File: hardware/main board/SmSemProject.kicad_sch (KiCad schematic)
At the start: 11 parts, among them J1 Conn_01x06, J2 Conn_01x06, J3 Conn_01x02

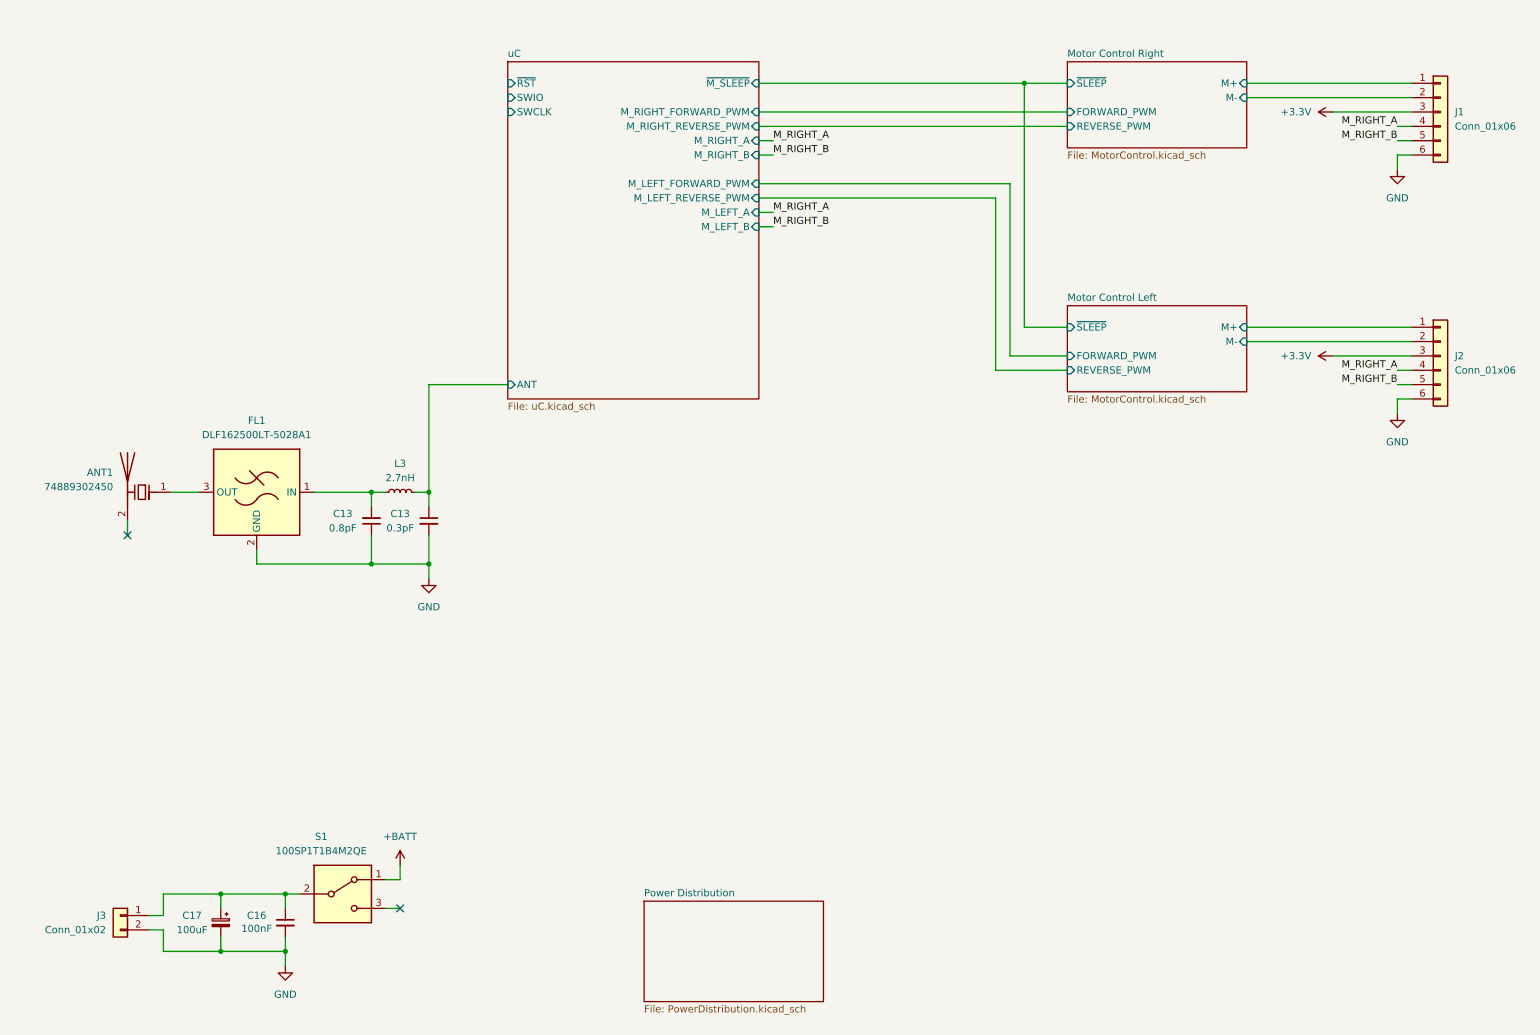
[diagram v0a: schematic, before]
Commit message: main board done, added front board projec
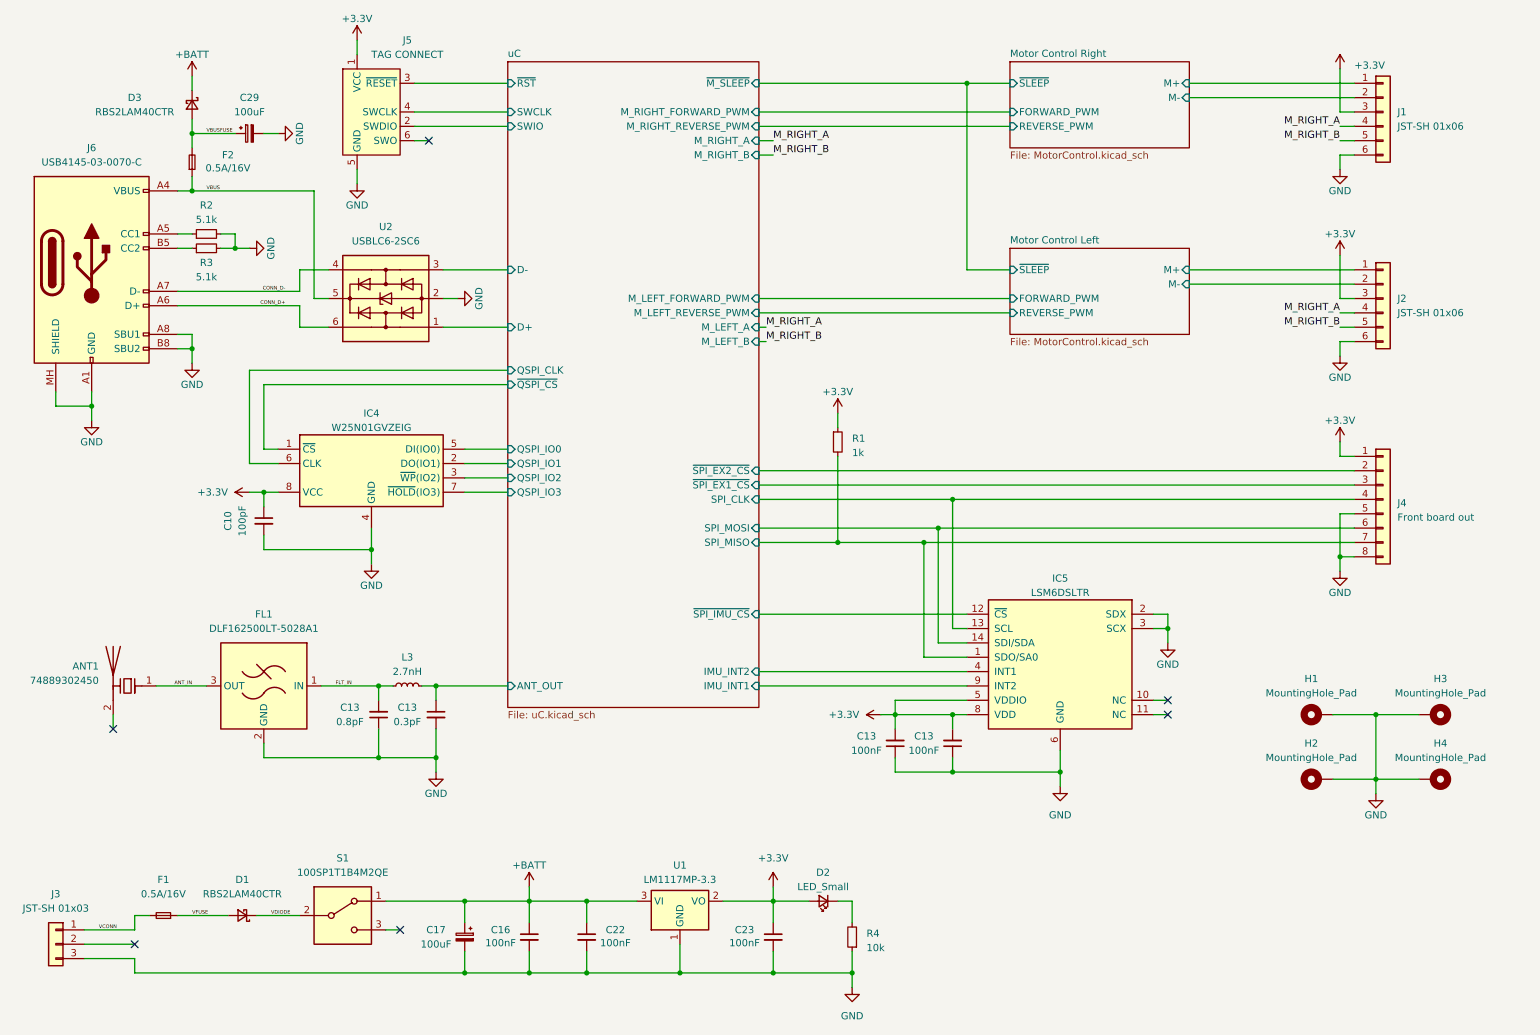
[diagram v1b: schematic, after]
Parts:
- removed J3: Conn_01x02, Connector_JST:JST_SH_BM02B-SRSS-TB_1x02-1MP_P1.00mm_Vertical, symbol Connector_Generic:Conn_01x02
- added C10: 100pF, Capacitor_SMD:C_0603_1608Metric, symbol Device:C_Small
- added C13 (x2), C22, C23: 100nF, Capacitor_SMD:C_0603_1608Metric, symbol Device:C_Small
- added C29: 100uF, Capacitor_SMD:CP_Elec_5x4.5, symbol Device:CP_Small
- added D1, D3: RBS2LAM40CTR, Diode_SMD:D_SOD-128, symbol Device:D_Schottky_Small
- added D2: LED_Small, LED_SMD:LED_0603_1608Metric, symbol Device:LED_Small
- added F1, F2: 0.5A/16V, Fuse:Fuse_1210_3225Metric, symbol Device:Fuse_Small
- added H1, H2, H3, H4: MountingHole_Pad, MountingHole:MountingHole_3.2mm_M3_Pad_Via, symbol Mechanical:MountingHole_Pad
- added IC4: W25N01GVZEIG, Samacsys:SON127P800X600X80-9N-D, symbol Samacsys_kicad_sym:W25N01GVZEIG
- added IC5: LSM6DSLTR, Samacsys:LSM6DSLTR, symbol Samacsys_kicad_sym:LSM6DSLTR
- added J3: JST-SH 01x03, Connector_JST:JST_SH_BM03B-SRSS-TB_1x03-1MP_P1.00mm_Vertical, symbol Connector_Generic:Conn_01x03
- added J4: Front board out, Connector_FFC-FPC:Molex_200528-0080_1x08-1MP_P1.00mm_Horizontal, symbol Connector_Generic:Conn_01x08
- added J5: TAG CONNECT, Connector:Tag-Connect_TC2030-IDC-FP_2x03_P1.27mm_Vertical, symbol Connector:Conn_ARM_SWD_TagConnect_TC2030
- added J6: USB4145-03-0070-C, Samacsys:USB4145030070C, symbol Samacsys_kicad_sym:USB4145-03-0070-C
- added R1: 1k, Resistor_SMD:R_0603_1608Metric, symbol Device:R_Small
- added R2, R3: 5.1k, Resistor_SMD:R_0603_1608Metric, symbol Device:R_Small
- added R4: 10k, Resistor_SMD:R_0603_1608Metric, symbol Device:R_Small
- added U1: LM1117MP-3.3, Package_TO_SOT_SMD:SOT-223-3_TabPin2, symbol Regulator_Linear:LM1117MP-3.3
- added U2: USBLC6-2SC6, Package_TO_SOT_SMD:SOT-23-6, symbol Power_Protection:USBLC6-2SC6
- J1, J2: value Conn_01x06 -> JST-SH 01x06
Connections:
- net +3.3V: now also C10.1, C13.2, C13.2, C23.1, D2.2 (A), IC4.8 (VCC), IC5.5 (VDDIO), IC5.8 (VDD), J4.1 (Pin_1), J5.1 (VCC), R1.1, U1.2 (VO)
- net +BATT: now also C16.1, C17.1, C22.1, D3.1 (K), U1.3 (VI)
- net GND: now also C10.2, C13.1, C13.1, C22.2, C23.2, C29.2, H1.1, H2.1, H3.1, H4.1, IC4.4 (GND), IC4.9 (EP), IC5.2 (SDX), IC5.3 (SCX), IC5.6 (GND), IC5.7 (GND), J3.3 (Pin_3), J4.5 (Pin_5), J4.8 (Pin_8), J5.5 (GND), J6.A1 (GND), J6.A12 (GND), J6.A8 (SBU1), J6.B1 (GND), J6.B12 (GND), J6.B8 (SBU2), J6.MH (SHIELD), R2.2, R3.2, R4.1, U1.1 (GND), U2.2 (GND)
- net uC/SWCLK: now also J5.4 (SWCLK)
- net uC/SWIO: now also J5.2 (SWDIO)
- net uC/~{RST}: now also J5.3 (~{RESET})
- net FLT_IN: now reaches C13.2, FL1.1 (IN), L3.2
- net ANT_IN: now reaches ANT1.1 (FEED), FL1.3 (OUT)
- net uC/ANT renamed uC/ANT_OUT
- new net: D2.1 (K), R4.2
- new net: J6.A5 (CC1), R2.1
- new net: J6.B5 (CC2), R3.1
- new net CONN_D+: J6.A6 (D+), J6.B6 (D+), U2.6 (I/O1)
- new net CONN_D-: J6.A7 (D-), J6.B7 (D-), U2.4 (I/O2)
- new net VBUS: F2.1, J6.A4 (VBUS), J6.A9 (VBUS), J6.B4 (VBUS), J6.B9 (VBUS), U2.5 (VBUS)
- new net VBUSFUSE: C29.1, D3.2 (A), F2.2
- new net VCONN: F1.2, J3.1 (Pin_1)
- new net VDIODE: D1.1 (K), S1.2 (B)
- new net VFUSE: D1.2 (A), F1.1
- new net uC/D+: U2.1 (I/O1)
- new net uC/D-: U2.3 (I/O2)
- new net uC/IMU_INT1: IC5.9 (INT2)
- new net uC/IMU_INT2: IC5.4 (INT1)
- new net uC/QSPI_CLK: IC4.6 (CLK)
- new net uC/QSPI_IO0: IC4.5 (DI(IO0))
- new net uC/QSPI_IO1: IC4.2 (DO(IO1))
- new net uC/QSPI_IO2: IC4.3 (~{WP}(IO2))
- new net uC/QSPI_IO3: IC4.7 (~{HOLD}(IO3))
- new net uC/SPI_CLK: IC5.13 (SCL), J4.4 (Pin_4)
- new net uC/SPI_MISO: IC5.1 (SDO/SA0), J4.7 (Pin_7), R1.2
- new net uC/SPI_MOSI: IC5.14 (SDI/SDA), J4.6 (Pin_6)
- new net uC/~{QSPI_CS}: IC4.1 (~{CS})
- new net uC/~{SPI_EX1_CS}: J4.3 (Pin_3)
- new net uC/~{SPI_EX2_CS}: J4.2 (Pin_2)
- new net uC/~{SPI_IMU_CS}: IC5.12 (~{CS})
- no-connect marks 2 -> 6
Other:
- removed sheet Power Distribution
- sheet uC ports: added ANT_OUT, D+, D-, IMU_INT1, IMU_INT2, QSPI_CLK, QSPI_IO0, QSPI_IO1, QSPI_IO2, QSPI_IO3, SPI_CLK, SPI_MISO, SPI_MOSI, ~{QSPI_CS}, ~{SPI_EX1_CS}, ~{SPI_EX2_CS}, ~{SPI_IMU_CS}; removed ANT
- moved on the sheet: ANT1, C13, C16, C17, FL1, J1, J2, L3, S1

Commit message: front board schematic done
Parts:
- removed J4: Front board out, Connector_FFC-FPC:Molex_200528-0080_1x08-1MP_P1.00mm_Horizontal, symbol Connector_Generic:Conn_01x08
- added J7: Conn_01x10, Connector_FFC-FPC:Molex_200528-0100_1x10-1MP_P1.00mm_Horizontal, symbol Connector_Generic:Conn_01x10
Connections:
- net Motor Control Right/M+ is gone; now on net M_LEFT+: J1.1 (Pin_1)
- net Motor Control Right/M- is gone; now on net M_LEFT-: J1.2 (Pin_2)
- net +3.3V: now also J7.1 (Pin_1)
- net GND: now also J7.10 (Pin_10), J7.7 (Pin_7)
- net M_RIGHT_A: no longer J2.4 (Pin_4)
- net M_RIGHT_B: no longer J2.5 (Pin_5)
- net Motor Control Left/M+ renamed M_LEFT+
- net Motor Control Left/M- renamed M_LEFT-
- net uC/SPI_CLK renamed SPI_CLK
- net SPI_CLK: now also J7.6 (Pin_6)
- net uC/SPI_MISO renamed SPI_MISO
- net SPI_MISO: now also J7.9 (Pin_9)
- net uC/SPI_MOSI renamed SPI_MOSI
- net SPI_MOSI: now also J7.8 (Pin_8)
- new net M_LEFT_A: J2.4 (Pin_4)
- new net M_LEFT_B: J2.5 (Pin_5)
- new net SPI_EX_INT1: J7.3 (Pin_3)
- new net SPI_EX_INT2: J7.2 (Pin_2)
- new net ~{SPI_EX1_CS}: J7.5 (Pin_5)
- new net ~{SPI_EX2_CS}: J7.4 (Pin_4)
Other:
- sheet uC ports: added SPI_EX_INT1, SPI_EX_INT2; removed none
- moved on the sheet: J2, R1

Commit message: front board layout & routing mostly done
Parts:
- J7: symbol Connector_Generic:Conn_01x10 -> Connector_Generic_MountingPin:Conn_01x10_MountingPin
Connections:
- net +3.3V: now also J7.10 (Pin_10); no longer J7.1 (Pin_1)
- net GND: now also J7.1 (Pin_1), J7.4 (Pin_4), J7.MP (MountPin); no longer J7.10 (Pin_10), J7.7 (Pin_7)
- net SPI_CLK: now also J7.5 (Pin_5); no longer J7.6 (Pin_6)
- net SPI_EX_INT1: now also J7.8 (Pin_8); no longer J7.3 (Pin_3)
- net SPI_EX_INT2: now also J7.9 (Pin_9); no longer J7.2 (Pin_2)
- net SPI_MISO: now also J7.2 (Pin_2); no longer J7.9 (Pin_9)
- net SPI_MOSI: now also J7.3 (Pin_3); no longer J7.8 (Pin_8)
- net ~{SPI_EX1_CS}: now also J7.6 (Pin_6); no longer J7.5 (Pin_5)
- net ~{SPI_EX2_CS}: now also J7.7 (Pin_7); no longer J7.4 (Pin_4)
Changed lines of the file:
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@@
+    (stroke (width 0) (type default))
+  )
+  (wire (pts (xy 256.54 118.11) (xy 256.54 120.65))
     (stroke (width 0) (type default))
   )
@@
     )
   )
-  (symbol (lib_id "Connector_Generic:Conn_01x10") (at 256.54 100.33 0) (unit 1)
-    (in_bom yes) (on_board yes) (dnp no) (fields_autoplaced)
-    (property "Reference" "J7" (at 259.08 100.965 0)
+  (symbol (lib_id "Connector_Generic_MountingPin:Conn_01x10_MountingPin") (at 256.54 102.87 0) (mirror x) (unit 1)
+    (in_bom yes) (on_board yes) (dnp no)
+    (property "Reference" "J7" (at 259.08 102.5144 0)
       (effects (font (size 1.27 1.27)) (justify left))
     )
-    (property "Value" "Conn_01x10" (at 259.08 103.505 0)
+    (property "Value" "Conn_01x10" (at 259.08 99.9744 0)
       (effects (font (size 1.27 1.27)) (justify left))
     )
-    (property "Footprint" "Connector_FFC-FPC:Molex_200528-0100_1x10-1MP_P1.00mm_Horizontal" (at 256.54 100.33 0)
-      (effects (font (size 1.27 1.27)) hide)
-    )
-    (property "Datasheet" "~" (at 256.54 100.33 0)
+    (property "Footprint" "Connector_FFC-FPC:Molex_200528-0100_1x10-1MP_P1.00mm_Horizontal" (at 256.54 102.87 0)
+      (effects (font (size 1.27 1.27)) hide)
+    )
+    (property "Datasheet" "~" (at 256.54 102.87 0)
       (effects (font (size 1.27 1.27)) hide)
     )
@@
     (pin "8")
     (pin "9")
+    (pin "MP")
     (instances
       (project "SmSemProject"
@@
         )
       )
+    )
+  )
+  (symbol (lib_id "power:GND") (at 256.54 120.65 0) (unit 1)
+    (in_bom yes) (on_board yes) (dnp no)
+    (property "Reference" "#PWR02" (at 256.54 127 0)
+      (effects (font (size 1.27 1.27)) hide)
+    )
+    (property "Value" "GND" (at 256.54 124.46 0)
+      (effects (font (size 1.27 1.27)))
+    )
+    (property "Footprint" "" (at 256.54 120.65 0)
+      (effects (font (size 1.27 1.27)) hide)
+    )
+    (property "Datasheet" "" (at 256.54 120.65 0)
+      (effects (font (size 1.27 1.27)) hide)
+    )
+    (pin "1")
+    (instances
+      (project "SmSemProject"
+        (path "/2d1fee9c-ff28-4ed3-bed9-80ad18eb590f"
+          (reference "#PWR02") (unit 1)
+        )
+      )

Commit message: all layouts and routings done
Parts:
- removed C22, C23: 100nF, Capacitor_SMD:C_0603_1608Metric, symbol Device:C_Small
- removed J5: TAG CONNECT, Connector:Tag-Connect_TC2030-IDC-FP_2x03_P1.27mm_Vertical, symbol Connector:Conn_ARM_SWD_TagConnect_TC2030
- removed S1: 100SP1T1B4M2QE, Samacsys:100SP1T1B4M2QE, symbol Samacsys_kicad_sym:100SP1T1B4M2QE
- added D8: LED_Small, LED_SMD:LED_0603_1608Metric, symbol Device:LED_Small
- added J4: FTSH-107-01-L-DV-K-A, Samacsys:FTSH-107-XX-YYY-DV-K-A, symbol Samacsys_kicad_sym:FTSH-107-01-L-DV-K-A
- added R12: 10k, Resistor_SMD:R_0603_1608Metric, symbol Device:R_Small
- C10: value 100pF -> 100nF
- J3: value JST-SH 01x03 -> JST_XH_B3B; footprint Connector_JST:JST_SH_BM03B-SRSS-TB_1x03-1MP_P1.00mm_Vertical -> Connector_JST:JST_XH_B3B-XH-A_1x03_P2.50mm_Vertical
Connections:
- net VDIODE is gone; now on net +BATT: D1.1 (K)
- net +3.3V: now also J4.3 (Pin_3)
- net +BATT: now also C29.1, D8.2 (A)
- net GND: now also J4.11 (Pin_11), J4.5 (Pin_5), J4.7 (Pin_7), R12.1
- net M_LEFT+: no longer J1.1 (Pin_1)
- net M_LEFT-: no longer J1.2 (Pin_2)
- net VBUSFUSE: no longer C29.1
- net uC/SWCLK: now also J4.6 (Pin_6)
- net uC/~{RST}: now also J4.12 (Pin_12)
- net M_LEFT_B: no longer names the net of J2.5 (Pin_5)
- net M_RIGHT_B: no longer names the net of J1.5 (Pin_5)
- new net: D8.1 (K), R12.2
- new net M_RIGHT+: J1.1 (Pin_1)
- new net M_RIGHT-: J1.2 (Pin_2)
- new net uC/SWDIO: J4.4 (Pin_4)
- new net uC/UART_RX: J4.13 (Pin_13)
- new net uC/UART_TX: J4.14 (Pin_14)
- no-connect marks 6 -> 11
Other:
- sheet Motor Control Left ports: added DIRECTION, PWM; removed FORWARD_PWM, REVERSE_PWM
- sheet Motor Control Right ports: added DIRECTION, PWM; removed FORWARD_PWM, REVERSE_PWM
- sheet uC ports: added M_LEFT_DIRECTION, M_LEFT_PWM, M_RIGHT_DIRECTION, M_RIGHT_PWM, SWDIO, UART_RX, UART_TX; removed M_LEFT_B, M_LEFT_FORWARD_PWM, M_LEFT_REVERSE_PWM, M_RIGHT_B, M_RIGHT_FORWARD_PWM, M_RIGHT_REVERSE_PWM, SWIO
- moved on the sheet: C16, C17, C29, D1, D2, D3, F1, F2, J3, J6, R2, R3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

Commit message: firmware - added common classes
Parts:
- ANT1, C17, C29, D1, D3, F1, F2, FL1, IC4, IC5, J4, J6, U2: Dodane do zamówienia (none) -> 1
- C10, C13, C16: Dodane do zamówienia (none) -> 20; Mouser Part Number (none) -> 963-EMK107B7104MA-T; Mouser Price/Stock (none) -> https://www.mouser.pl/ProductDetail/TAIYO-YUDEN/EMK107B7104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
- C13: Dodane do zamówienia (none) -> 2; Mouser Part Number (none) -> 581-600S0R8AW; Mouser Price/Stock (none) -> https://www.mouser.pl/ProductDetail/KYOCERA-AVX/600S0R8AW25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
- C13: Dodane do zamówienia (none) -> 2; Mouser Part Number (none) -> 581-600S0R3AT250TV; Mouser Price/Stock (none) -> https://www.mouser.pl/ProductDetail/581-600S0R3AT250TV
- D2, D8: Dodane do zamówienia (none) -> 20; Mouser Part Number (none) -> --different--
- H1, H2, H3, H4: Manufacturer_Part_Number (none) -> --; Mouser Part Number (none) -> --
- J1, J2: Dodane do zamówienia (none) -> 1; Mouser Part Number (none) -> BM06B-SRSS-TB; Mouser Price/Stock (none) -> https://www.tme.eu/pl/details/bm06b-srss-tb/zlacza-sygnalow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
- J3: Dodane do zamówienia (none) -> 1; Mouser Part Number (none) -> B3B-XH-A; Mouser Price/Stock (none) -> https://www.tme.eu/pl/details/b3b-xh-a/zlacza-sygnalowe-ras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
- J7: Dodane do zamówienia (none) -> 3; Manufacturer_Part_Number (none) -> 200528-0100; Mouser Part Number (none) -> 200528-0100; Mouser Price/Stock (none) -> https://www.mouser.pl/ProductDetail/Molex/200528-0100?qs=0l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
- L3: Dodane do zamówienia (none) -> 2; Mouser Part Number (none) -> 710-7447860027G; Mouser Price/Stock (none) -> https://www.mouser.pl/ProductDetail/Wurth-Elektronik/744786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
- R1: Dodane do zamówienia (none) -> 10; Mouser Part Number (none) -> CRCW06031K00FKECC; Mouser Price/Stock (none) -> https://www.mouser.pl/ProductDetail/Vishay-Dale/CRCW06031K0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
- R12, R4: Dodane do zamówienia (none) -> 10; Mouser Part Number (none) -> CRGCQ0603F10K; Mouser Price/Stock (none) -> https://www.mouser.pl/ProductDetail/TE-Connectivity-Holswor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
- R2, R3: Dodane do zamówienia (none) -> 10; Mouser Part Number (none) -> RC0603FR-075K1P; Mouser Price/Stock (none) -> https://www.mouser.pl/ProductDetail/YAGEO/RC0603FR-075K1P?q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
- U1: Dodane do zamówienia (none) -> 1; Mouser Part Number (none) -> LM1117MPX-3.3/NOPB; Mouser Price/Stock (none) -> https://www.mouser.pl/ProductDetail/Texas-Instruments/LM111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
